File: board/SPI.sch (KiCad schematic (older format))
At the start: 32 parts, among them P3 CONN_7X2, U11 MICRO_SD, U17 FXO-HC536R, U18 FXO-HC536R, U19 FXO-HC536R, U3 W25Q128FVEIG

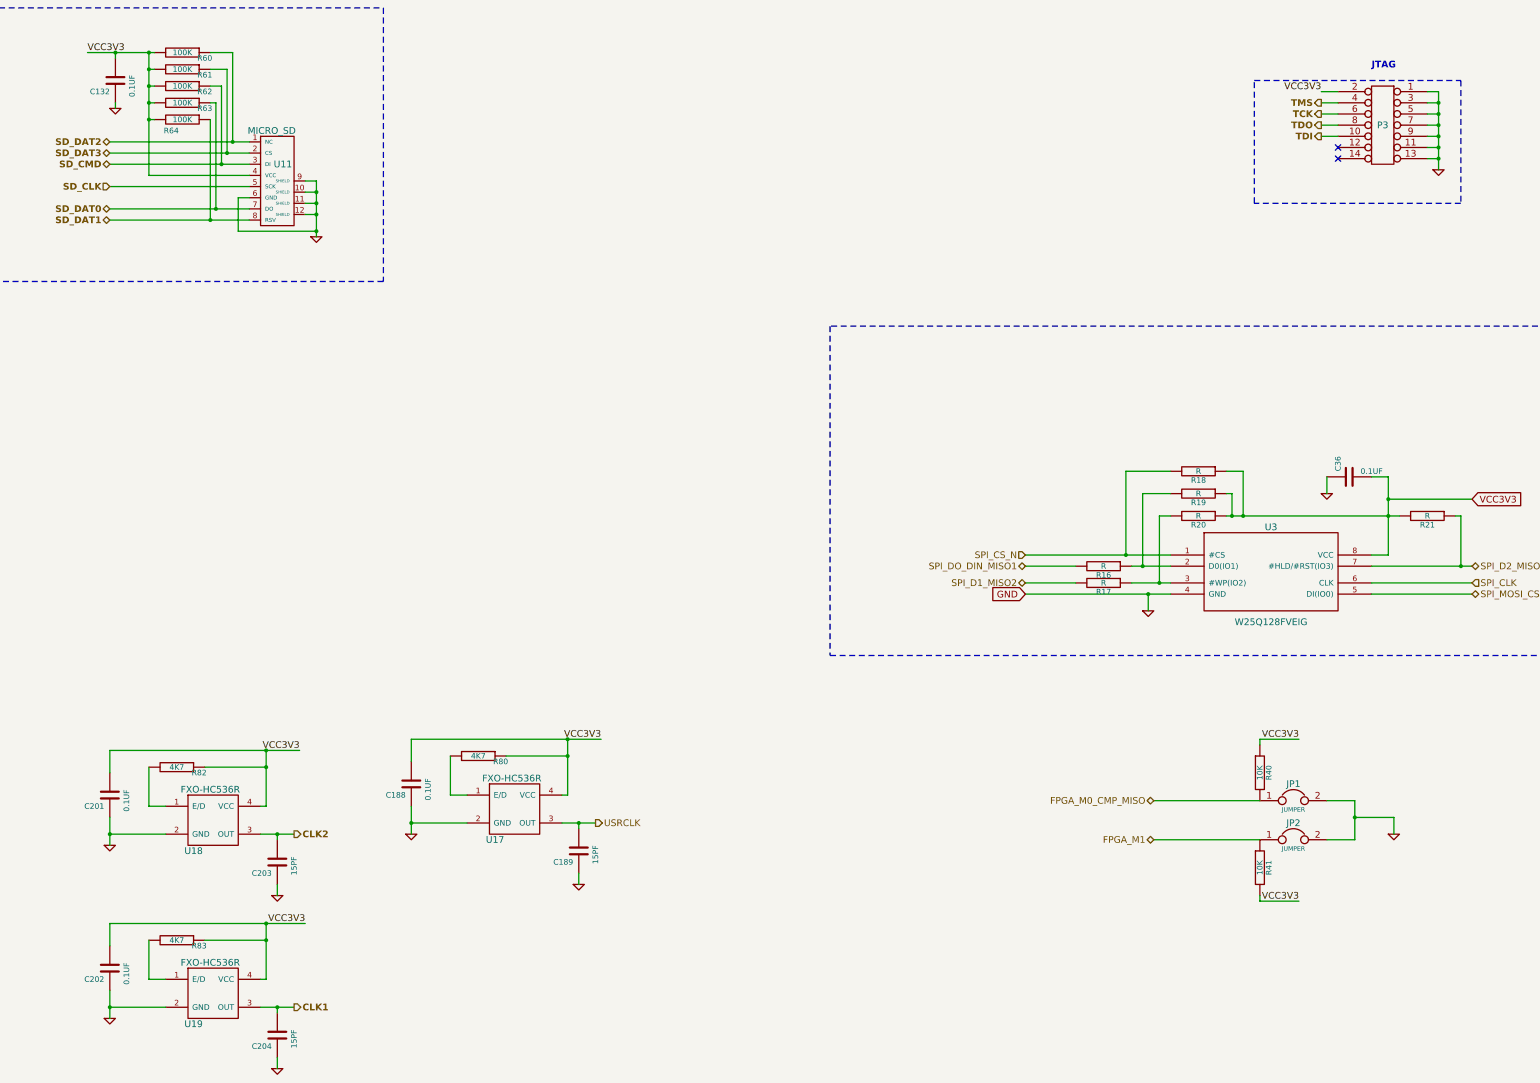
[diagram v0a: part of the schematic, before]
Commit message: Issue #1458 - HDMI RX TX pins added, Cypress added, DDR added
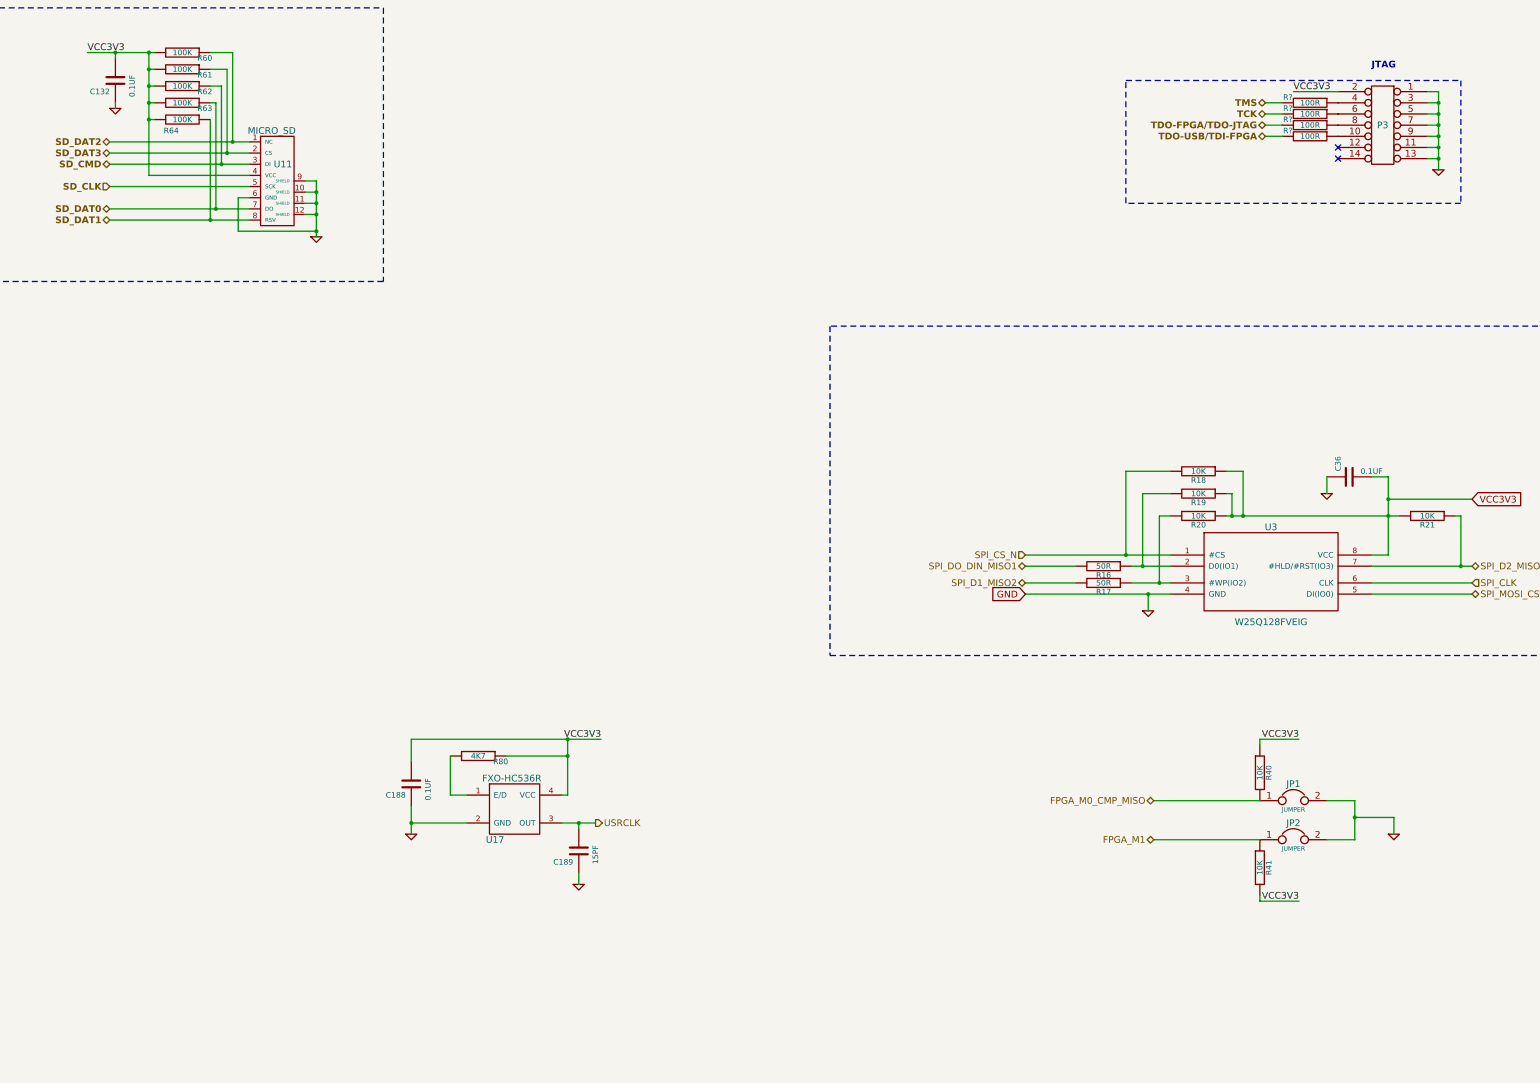
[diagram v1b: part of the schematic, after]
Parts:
- removed C201, C202: 0.1UF, symbol C
- removed C203, C204: 15PF, symbol C
- removed R82, R83: 4K7, symbol R
- removed U18, U19: FXO-HC536R, ~, symbol FXO-HC536R
- added R? (x4): 100R, symbol R
- R16, R17: value R -> 50R
- R18, R19, R20, R21: value R -> 10K
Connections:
- net TCK: now also R?.2; no longer P3.6 (P6)
- net TMS: now also R?.2; no longer P3.4 (P4)
- net TDI: no longer names the net of P3.10
- net TDI: now also R?.1
- net TDO: no longer names the net of P3.8 (P8)
- net TDO: now also R?.1
- new net: P3.4 (P4), R?.1
- new net: P3.6 (P6), R?.1
- new net TDO-FPGA/TDO-JTAG: R?.2
- new net TDO-USB/TDI-FPGA: R?.2

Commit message: Issue #1458 - USB2.0
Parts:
- added C?: 0.1UF, symbol C
- added R?: 27R, ~, symbol R
- added U?: USB3340, symbol USB3340
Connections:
- net GND: now also C?.2, U?.33 (GND_PAD)
- new net: R?.2, U?.1 (CLKOUT)
- new net USB_CLKOUT: R?.1
- new net USB_DATA0: U?.3 (DATA0)
- new net USB_DATA1: U?.4 (DATA1)
- new net USB_DATA2: U?.5 (DATA2)
- new net USB_DATA3: U?.6 (DATA3)
- new net USB_DATA4: U?.7 (DATA4)
- new net USB_DATA5: U?.9 (DATA5)
- new net USB_DATA6: U?.10 (DATA6)
- new net USB_DATA7: U?.13 (DATA7)
- new net USB_DIR: U?.31 (DIR)
- new net USB_NXT: U?.2 (NXT)
- new net USB_REFCLK: U?.26 (REFCLK)
- new net USB_REFSEL0: U?.8 (REFSEL0)
- new net USB_REFSEL1: U?.11 (REFSEL1)
- new net USB_REFSEL2: U?.14 (REFSEL2)
- new net USB_RESETB: U?.27 (RESETB)
- new net USB_STP: U?.29 (STP)
- no-connect marks 2 -> 5
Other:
- moved on the sheet: C132, C188, C189, C36, JP1, JP2, P3, R16, R17, R18, R19, R20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

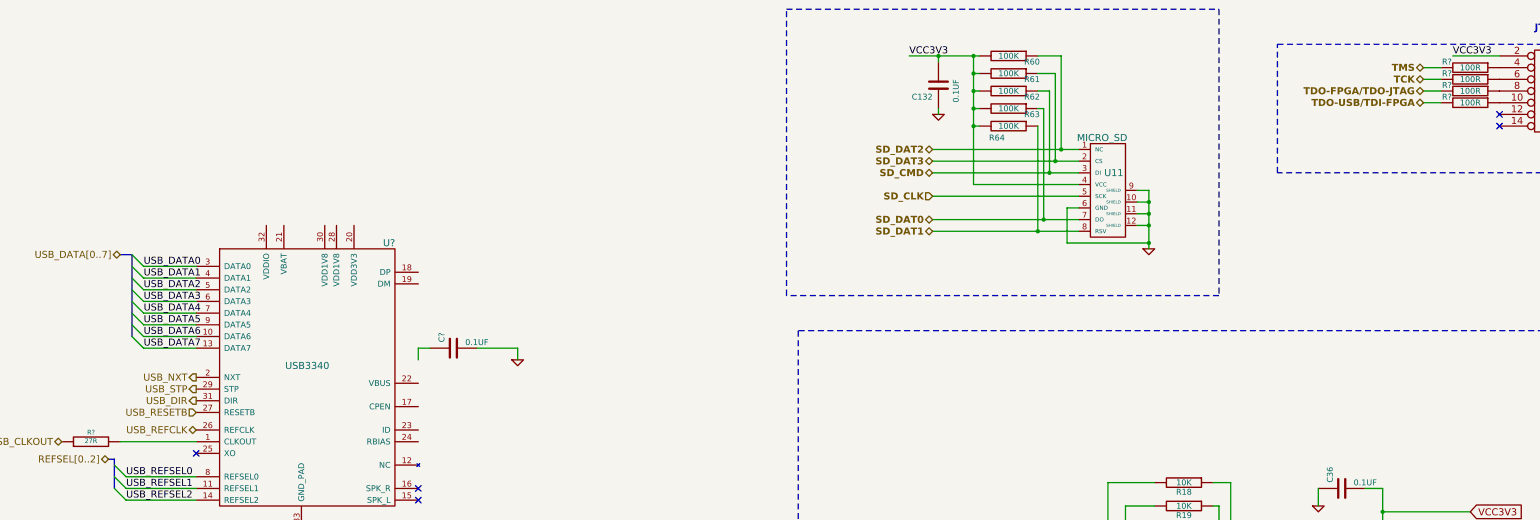
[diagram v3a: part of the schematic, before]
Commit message: Issue #1471 - HDMI Sheet changes
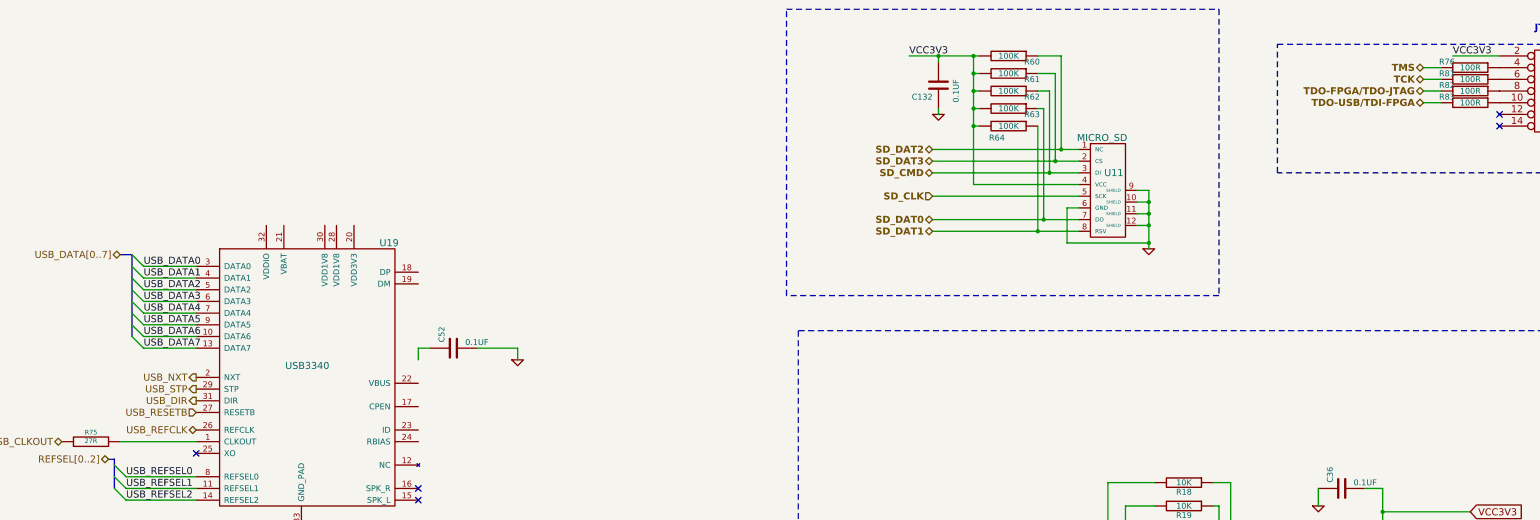
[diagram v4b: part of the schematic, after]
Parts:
- gave numbers to parts that had none: 7
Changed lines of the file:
@@
 Sheet 9 11
 Title "HDMI2USB"
-Date "29 dec 2014"
+Date "30 dec 2014"
 Rev "Rev2"
 Comp ""
@@
 $EndComp
 $Comp
-L GND #PWR014
+L GND #PWR34
 U 1 1 52D67B63
 P 11300 6050
-F 0 "#PWR014" H 11300 6050 30  0001 C CNN
+F 0 "#PWR34" H 11300 6050 30  0001 C CNN
 F 1 "GND" H 11300 5980 30  0001 C CNN
 F 2 "" H 11300 6050 60  0000 C CNN
@@
 $EndComp
 $Comp
-L GND #PWR015
+L GND #PWR36
 U 1 1 52D67F2B
 P 12900 5000
-F 0 "#PWR015" H 12900 5000 30  0001 C CNN
+F 0 "#PWR36" H 12900 5000 30  0001 C CNN
 F 1 "GND" H 12900 4930 30  0001 C CNN
 F 2 "" H 12900 5000 60  0000 C CNN
@@
 FPGA_M1
 $Comp
-L GND #PWR016
+L GND #PWR35
 U 1 1 52E410EA
 P 11450 2800
-F 0 "#PWR016" H 11450 2800 30  0001 C CNN
+F 0 "#PWR35" H 11450 2800 30  0001 C CNN
 F 1 "GND" H 11450 2730 30  0001 C CNN
 F 2 "" H 11450 2800 60  0000 C CNN
@@
 $EndComp
 $Comp
-L GND #PWR017
+L GND #PWR32
 U 1 1 52E4224F
 P 9650 1650
-F 0 "#PWR017" H 9650 1650 30  0001 C CNN
+F 0 "#PWR32" H 9650 1650 30  0001 C CNN
 F 1 "GND" H 9650 1580 30  0001 C CNN
 F 2 "" H 9650 1650 60  0000 C CNN
@@
 JTAG\n
 $Comp
-L GND #PWR018
+L GND #PWR37
 U 1 1 52E36A0E
 P 15350 1850
-F 0 "#PWR018" H 15350 1850 30  0001 C CNN
+F 0 "#PWR37" H 15350 1850 30  0001 C CNN
 F 1 "GND" H 15350 1780 30  0001 C CNN
 F 2 "" H 15350 1850 60  0000 C CNN
@@
 $EndComp
 $Comp
-L GND #PWR019
+L GND #PWR31
 U 1 1 52E638C7
 P 9350 7750
-F 0 "#PWR019" H 9350 7750 30  0001 C CNN
+F 0 "#PWR31" H 9350 7750 30  0001 C CNN
 F 1 "GND" H 9350 7680 30  0001 C CNN
 F 2 "" H 9350 7750 60  0000 C CNN
@@
 $EndComp
 $Comp
-L GND #PWR020
+L GND #PWR33
 U 1 1 530C0275
 P 10850 8200
-F 0 "#PWR020" H 10850 8200 30  0001 C CNN
+F 0 "#PWR33" H 10850 8200 30  0001 C CNN
 F 1 "GND" H 10850 8130 30  0001 C CNN
 F 2 "" H 10850 8200 60  0000 C CNN
@@
 VCC3V3
 $Comp
-L GND #PWR025
+L GND #PWR38
 U 1 1 5392B9BD
 P 15600 7800
-F 0 "#PWR025" H 15600 7800 30  0001 C CNN
+F 0 "#PWR38" H 15600 7800 30  0001 C CNN
 F 1 "GND" H 15600 7730 30  0001 C CNN
 F 2 "" H 15600 7800 60  0000 C CNN
@@
 $EndComp
 $Comp
-L R R?
+L R R76
 U 1 1 54929477
 P 14200 1250
-F 0 "R?" V 14150 1050 50  0000 C CNN
+F 0 "R76" V 14150 1050 50  0000 C CNN
 F 1 "100R" V 14200 1250 50  0000 C CNN
 F 2 "" H 14200 1250 60  0000 C CNN
@@
 $EndComp
 $Comp
-L R R?
+L R R81
 U 1 1 5492948C
 P 14200 1350
-F 0 "R?" V 14150 1150 50  0000 C CNN
+F 0 "R81" V 14150 1150 50  0000 C CNN
 F 1 "100R" V 14200 1350 50  0000 C CNN
 F 2 "" H 14200 1350 60  0000 C CNN
@@
 $EndComp
 $Comp
-L R R?
+L R R82
 U 1 1 549294A6
 P 14200 1450
-F 0 "R?" V 14150 1250 50  0000 C CNN
+F 0 "R82" V 14150 1250 50  0000 C CNN
 F 1 "100R" V 14200 1450 50  0000 C CNN
 F 2 "" H 14200 1450 60  0000 C CNN
@@
 $EndComp
 $Comp
-L R R?
+L R R83
 U 1 1 549294AC
 P 14200 1550
-F 0 "R?" V 14150 1350 50  0000 C CNN
+F 0 "R83" V 14150 1350 50  0000 C CNN
 F 1 "100R" V 14200 1550 50  0000 C CNN
 F 2 "" H 14200 1550 60  0000 C CNN
@@
 $EndComp
 $Comp
-L USB3340 U?
+L USB3340 U19
 U 1 1 54949360
 P 4200 4000
-F 0 "U?" H 4950 5250 60  0000 C CNN
+F 0 "U19" H 4950 5250 60  0000 C CNN
 F 1 "USB3340" H 4250 4200 60  0000 C CNN
 F 2 "" H 3900 4000 60  0000 C CNN
@@
 USB_NXT
 $Comp
-L C C?
+L C C52
 U 1 1 5494E575
 P 5500 3650
-F 0 "C?" H 5550 3750 50  0000 L CNN
+F 0 "C52" H 5550 3750 50  0000 L CNN
 F 1 "0.1UF" V 5550 3350 50  0000 L CNN
 F 2 "" H 5500 3650 60  0000 C CNN
@@
 $EndComp
 $Comp
-L GND #PWR?
+L GND #PWR30
 U 1 1 5494E6B5
 P 6050 3750
-F 0 "#PWR?" H 6050 3750 30  0001 C CNN
+F 0 "#PWR30" H 6050 3750 30  0001 C CNN
 F 1 "GND" H 6050 3680 30  0001 C CNN
 F 2 "" H 6050 3750 60  0000 C CNN
@@
 NoConn ~ 3300 4550
 $Comp
-L R R?
+L R R75
 U 1 1 54951BE3
 P 2400 4450
-F 0 "R?" V 2480 4450 40  0000 C CNN
+F 0 "R75" V 2480 4450 40  0000 C CNN
 F 1 "27R" V 2407 4451 40  0000 C CNN
 F 2 "~" V 2330 4450 30  0000 C CNN
@@
 NoConn ~ 5200 4950
 $Comp
-L GND #PWR?
+L GND #PWR29
 U 1 1 54956584
 P 4200 5250
-F 0 "#PWR?" H 4200 5250 30  0001 C CNN
+F 0 "#PWR29" H 4200 5250 30  0001 C CNN
 F 1 "GND" H 4200 5180 30  0001 C CNN
 F 2 "" H 4200 5250 60  0000 C CNN

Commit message: Issue #1471 - usb Sheet changes
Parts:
- removed C52: 0.1UF, symbol C
- removed R75: 27R, ~, symbol R
- removed U19: USB3340, symbol USB3340
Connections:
- no-connect marks 5 -> 2
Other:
- note added: "100MHz"
- moved on the sheet: C132, C188, C189, C36, JP1, JP2, P3, R16, R17, R18, R19, R20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
